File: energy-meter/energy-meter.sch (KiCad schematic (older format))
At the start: 9 parts, among them J1 Screw_Terminal_01x04, K1 G5RL-U1A-E, P1 PineNut, T1 AP-2500, T2 BV 202 0154, U9 GD32VF103

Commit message: continue changing schematic
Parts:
- removed R? (x3): 50R, 0.1%, Resistor_SMD:R_0603_1608Metric_Pad1.05x0.95mm_HandSolder, symbol Device:R
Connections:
- net CURRENT0: now reaches T1.1
- net CURRENT1: now reaches T1.2
- net VOLTAGE1: now reaches T2.6 (SA)
- net VOLTAGE0: now reaches T2.7 (SB)
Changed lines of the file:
@@
 F7 "TEMP1" I L 4500 5750 50
 F8 "VDDA" I R 5600 4950 50
-F9 "OUT0B" I R 5600 5350 50
-F10 "OUT1" I R 5600 5450 50
-F11 "IN1" I R 5600 5550 50
-F12 "IN0" I R 5600 5650 50
-F13 "DAC0" I L 4500 5550 50
-F14 "DAC1" I L 4500 5650 50
-F15 "OUT1_to_MCU" I L 4500 6150 50
-F16 "SCL" I L 4500 5150 50
-F17 "SDA" I L 4500 5250 50
-F18 "U10B_10k" I L 4500 6250 50
-F19 "OUT01_SHORT" I L 4500 6350 50
+F9 "DAC0" I L 4500 5550 50
+F10 "DAC1" I L 4500 5650 50
+F11 "OUT1_to_MCU" I L 4500 6150 50
+F12 "SCL" I L 4500 5150 50
+F13 "SDA" I L 4500 5250 50
+F14 "U10B_10k" I L 4500 6250 50
+F15 "OUT01_SHORT" I L 4500 6350 50
+F16 "CURRENT1" I R 5600 5600 50
+F17 "CURRENT0" I R 5600 5500 50
+F18 "VOLTAGE1" I R 5600 5400 50
+F19 "VOLTAGE0" I R 5600 5300 50
 $EndSheet
 $Comp
@@
 Text GLabel 7100 2950 0    50   Input ~ 0
 N
-$Comp
-L Device:R R?
-U 1 1 6094B5A5
-P 8300 3400
-AR Path="/602A3FC4/6094B5A5" Ref="R?"  Part="1"
-AR Path="/60514CC5/6094B5A5" Ref="R?"  Part="1"
-AR Path="/607B74C2/6094B5A5" Ref="R?"  Part="1"
-AR Path="/6094B5A5" Ref="R?"  Part="1"
-F 0 "R?" V 8093 3400 50  0000 C CNN
-F 1 "50R, 0.1%" V 8184 3400 50  0000 C CNN
-F 2 "Resistor_SMD:R_0603_1608Metric_Pad1.05x0.95mm_HandSolder" V 8230 3400 50  0001 C CNN
-F 3 "~" H 8300 3400 50  0001 C CNN
-	1    8300 3400
-	1    0    0    -1
-$EndComp
 Wire Wire Line
 	7600 3700 8300 3700
 Wire Wire Line
-	8300 3700 8300 3550
-Wire Wire Line
 	7600 3100 8300 3100
 Wire Wire Line
-	8300 3100 8300 3250
-$Comp
-L Device:R R?
-U 1 1 6094D567
-P 8150 2550
-AR Path="/602A3FC4/6094D567" Ref="R?"  Part="1"
-AR Path="/60514CC5/6094D567" Ref="R?"  Part="1"
-AR Path="/607B74C2/6094D567" Ref="R?"  Part="1"
-AR Path="/6094D567" Ref="R?"  Part="1"
-F 0 "R?" V 7943 2550 50  0000 C CNN
-F 1 "50R, 0.1%" V 8034 2550 50  0000 C CNN
-F 2 "Resistor_SMD:R_0603_1608Metric_Pad1.05x0.95mm_HandSolder" V 8080 2550 50  0001 C CNN
-F 3 "~" H 8150 2550 50  0001 C CNN
-	1    8150 2550
-	0    1    1    0
-$EndComp
-$Comp
-L Device:R R?
-U 1 1 6094DE74
-P 8400 2750
-AR Path="/602A3FC4/6094DE74" Ref="R?"  Part="1"
-AR Path="/60514CC5/6094DE74" Ref="R?"  Part="1"
-AR Path="/607B74C2/6094DE74" Ref="R?"  Part="1"
-AR Path="/6094DE74" Ref="R?"  Part="1"
-F 0 "R?" V 8193 2750 50  0000 C CNN
-F 1 "50R, 0.1%" V 8284 2750 50  0000 C CNN
-F 2 "Resistor_SMD:R_0603_1608Metric_Pad1.05x0.95mm_HandSolder" V 8330 2750 50  0001 C CNN
-F 3 "~" H 8400 2750 50  0001 C CNN
-	1    8400 2750
-	-1   0    0    1
-$EndComp
-Wire Wire Line
-	7900 2950 8400 2950
-Wire Wire Line
-	8400 2950 8400 2900
-Wire Wire Line
-	8400 2600 8400 2550
-Wire Wire Line
-	8400 2550 8300 2550
-Wire Wire Line
-	8000 2550 7900 2550
+	7900 2950 8300 2950
+Text Label 6050 5300 2    50   ~ 0
+VOLTAGE0
+Text Label 6050 5400 2    50   ~ 0
+VOLTAGE1
+Text Label 6050 5500 2    50   ~ 0
+CURRENT0
+Text Label 6050 5600 2    50   ~ 0
+CURRENT1
+Wire Wire Line
+	5600 5300 6050 5300
+Wire Wire Line
+	6050 5400 5600 5400
+Wire Wire Line
+	6050 5500 5600 5500
+Wire Wire Line
+	6050 5600 5600 5600
+Text Label 8300 2550 2    50   ~ 0
+VOLTAGE0
+Text Label 8300 2950 2    50   ~ 0
+VOLTAGE1
+Text Label 8300 3100 2    50   ~ 0
+CURRENT0
+Text Label 8300 3700 2    50   ~ 0
+CURRENT1
+Wire Wire Line
+	7900 2550 8300 2550
 $EndSCHEMATC

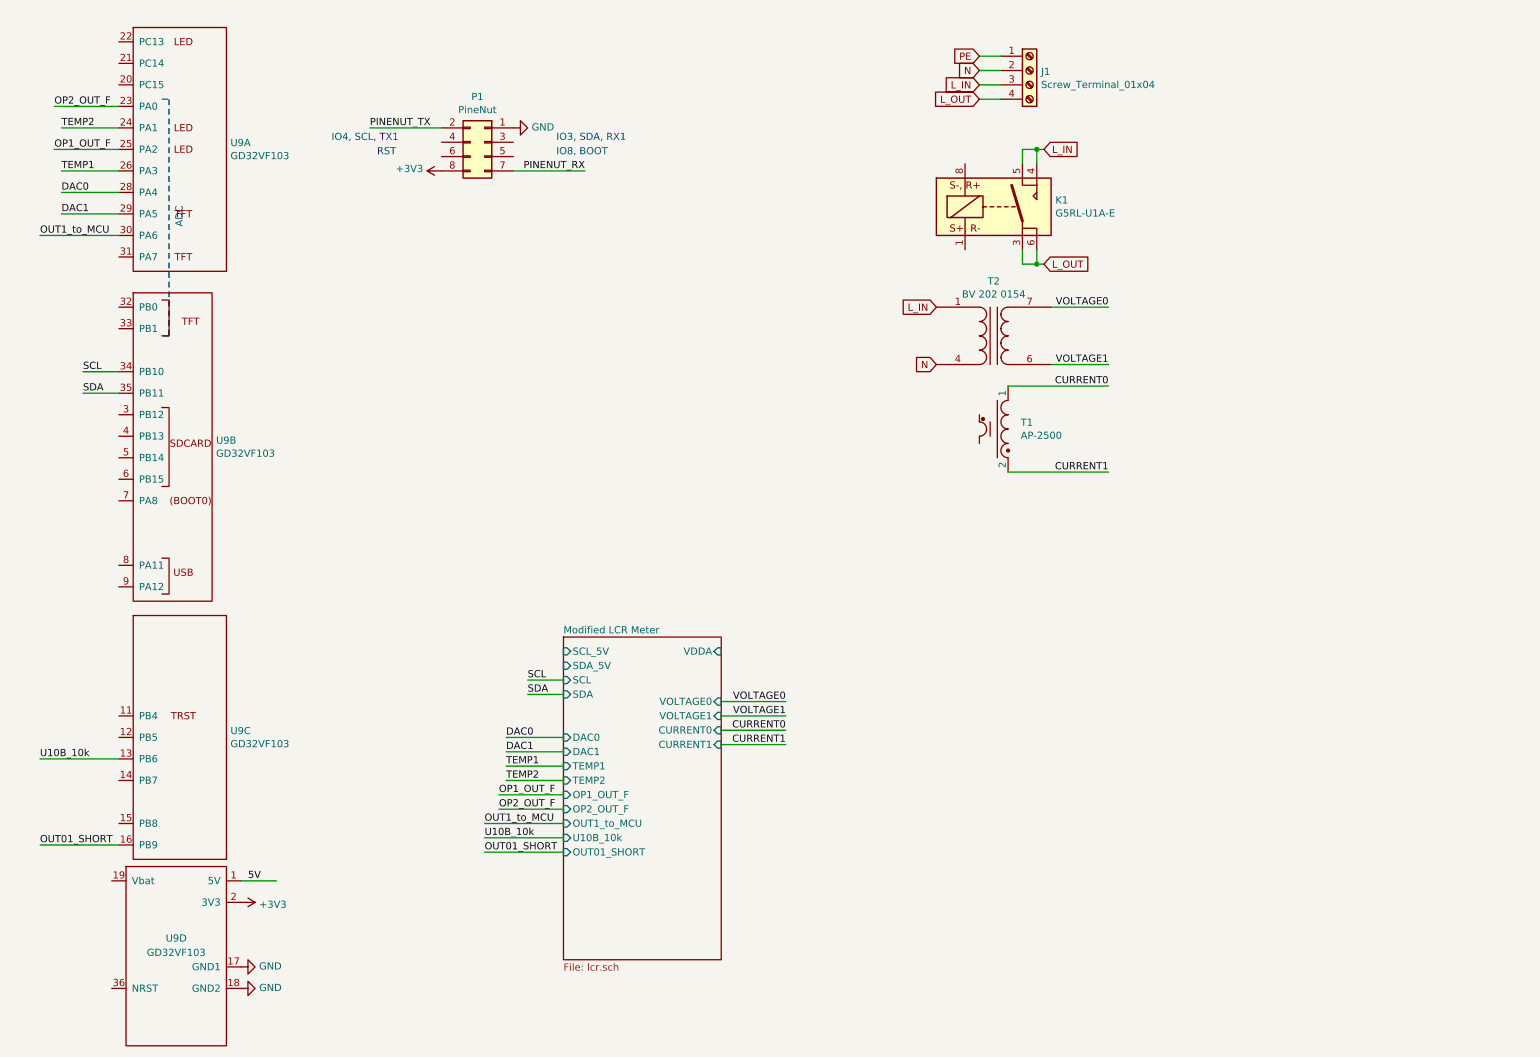
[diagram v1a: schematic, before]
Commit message: remove two of the opamps
We can measure the voltage without an amplifier so let's do it. The other
was used for the LCR outputs, which we don't have here.
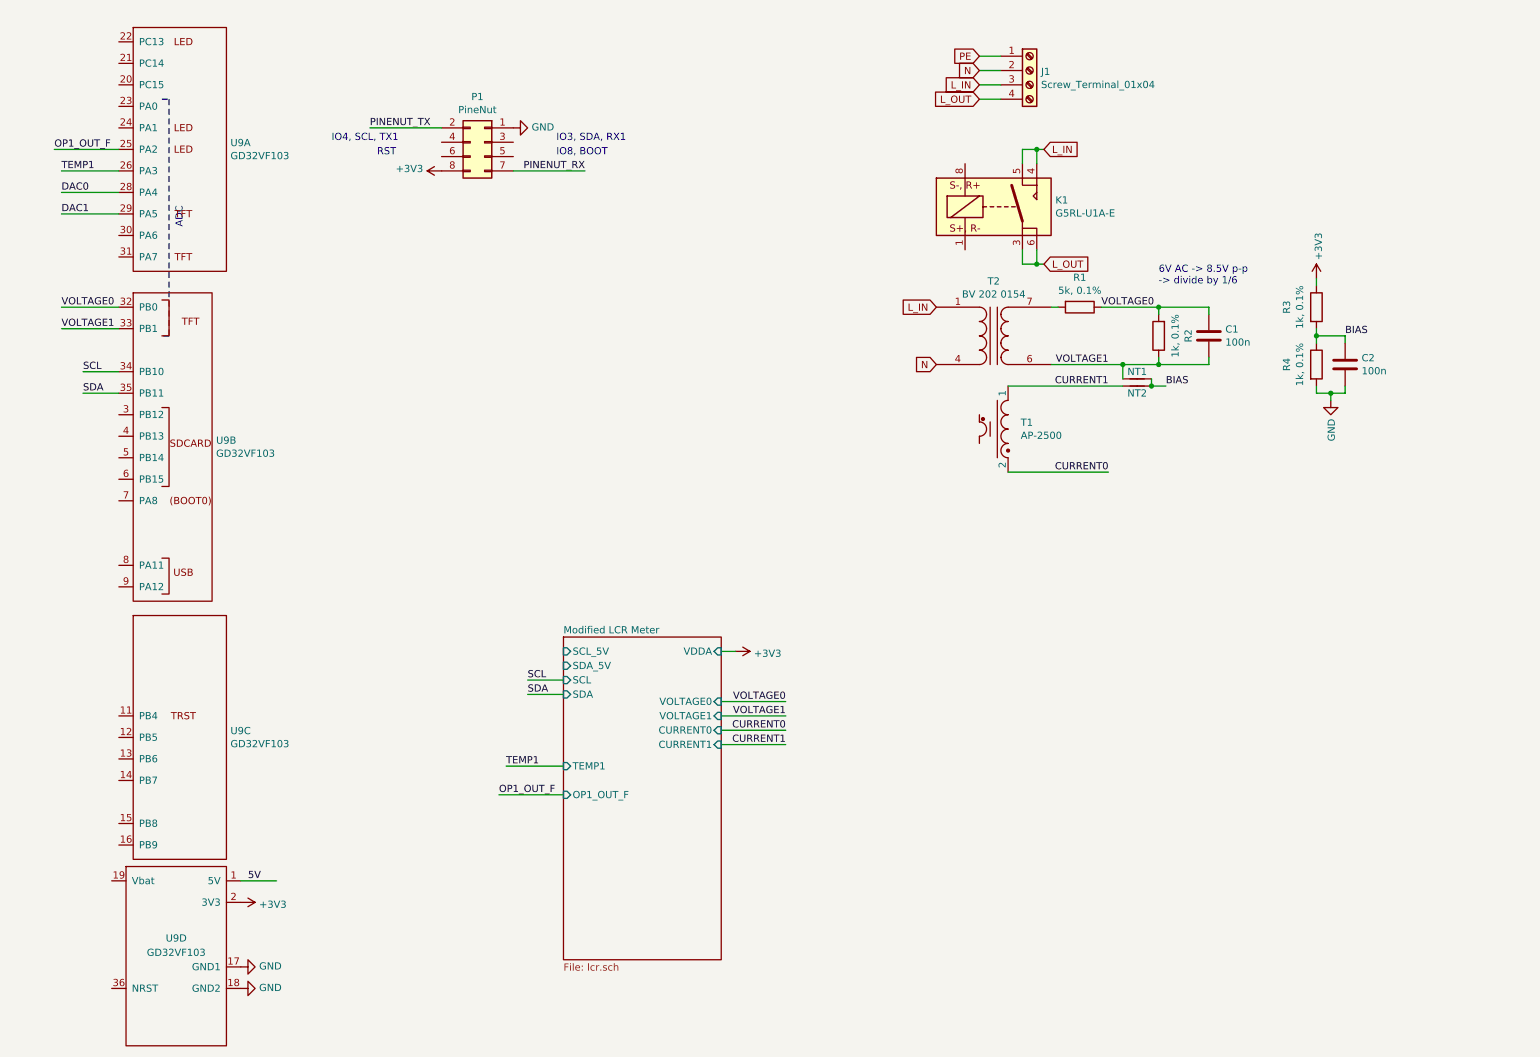
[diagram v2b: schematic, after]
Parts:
- added C1, C2: 100n, Capacitor_SMD:C_0603_1608Metric_Pad1.05x0.95mm_HandSolder, symbol Device:C
- added NT1, NT2: Net-Tie_2, NetTie:NetTie-2_SMD_Pad0.5mm, symbol Device:Net-Tie_2
- added R1: 5k, 0.1%, Resistor_SMD:R_0603_1608Metric_Pad1.05x0.95mm_HandSolder, symbol Device:R
- added R2, R3, R4: 1k, 0.1%, Resistor_SMD:R_0603_1608Metric_Pad1.05x0.95mm_HandSolder, symbol Device:R
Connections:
- net +3V3: now also R3.1
- net CURRENT0: now also T1.2; no longer T1.1
- net CURRENT1: now also T1.1, NT2.1; no longer T1.2
- net GND: now also C2.2, R4.2
- net VOLTAGE0: now also U9.32 (PB0), C1.1, R1.1, R2.2; no longer T2.7 (SB)
- net VOLTAGE1: now also U9.33 (PB1), C1.2, NT1.2, R2.1
- net OP2_OUT_F: no longer names the net of U9.23 (PA0)
- net OUT01_SHORT: no longer names the net of U9.16 (PB9)
- net OUT1_to_MCU: no longer names the net of U9.30 (PA6)
- net TEMP2: no longer names the net of U9.24 (PA1)
- net U10B_10k: no longer names the net of U9.13 (PB6)
- new net: R1.2, T2.7 (SB)
- new net BIAS: C2.1, NT1.1, NT2.2, R3.2, R4.1
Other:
- note added: "6V AC -> 8.5V p-p\n-> divide by 1/6"

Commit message: everything done except current measurement
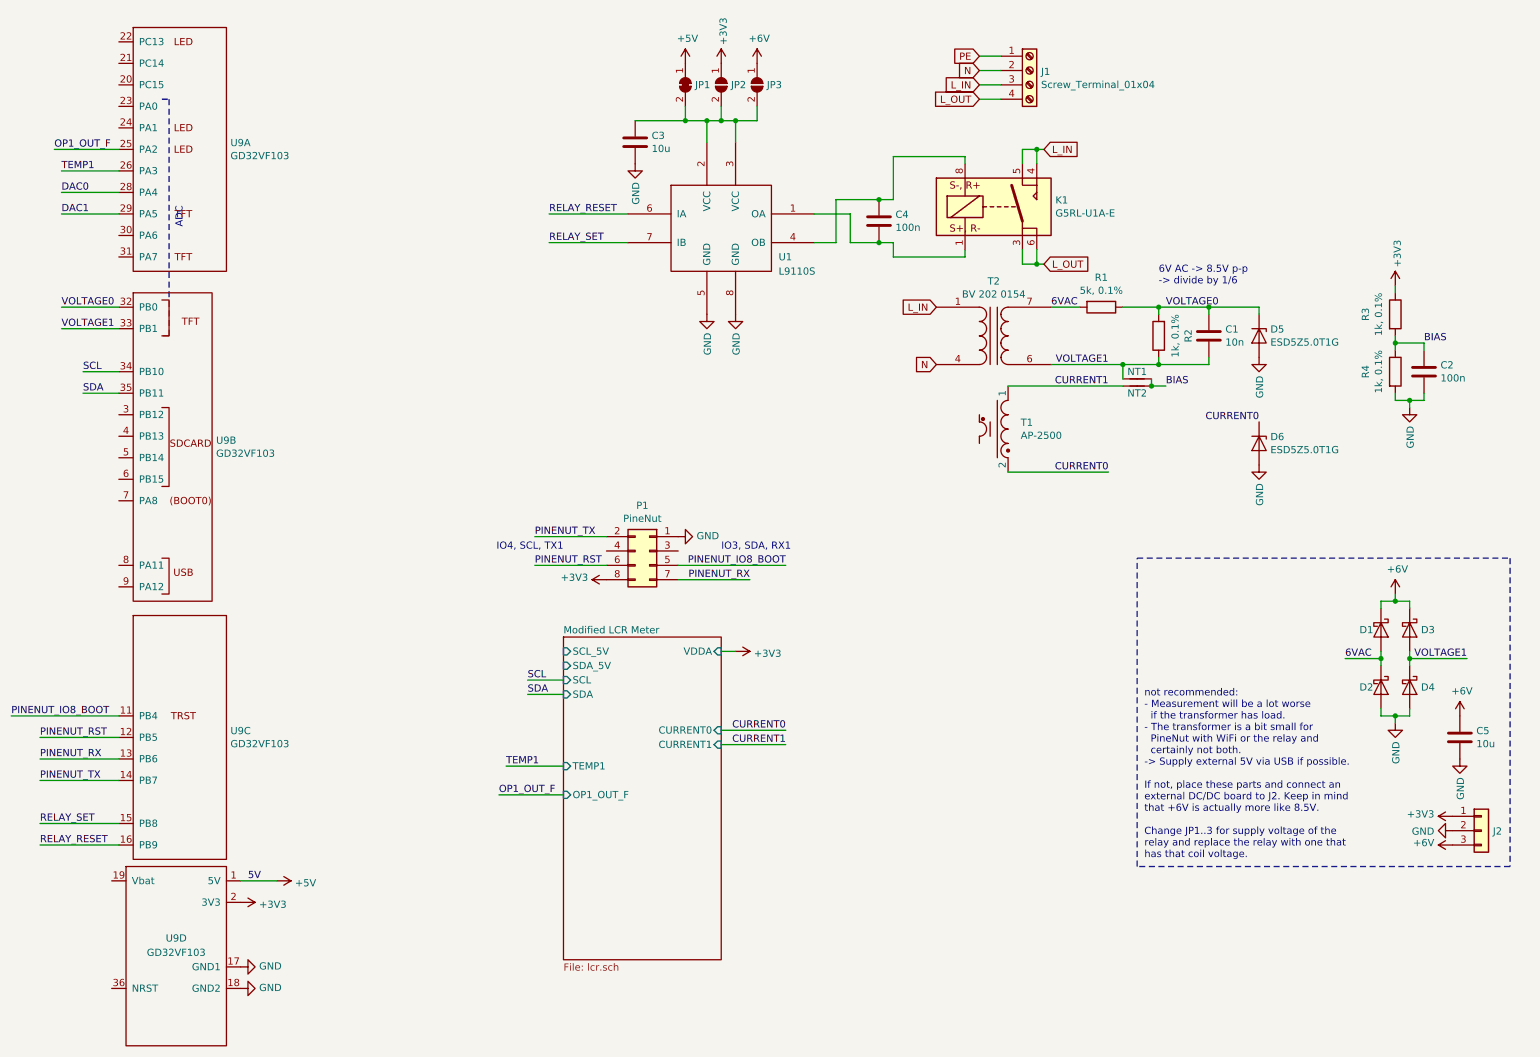
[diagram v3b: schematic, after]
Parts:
- added C3, C5: 10u, Capacitor_SMD:C_0805_2012Metric_Pad1.15x1.40mm_HandSolder, symbol Device:C
- added C4: 100n, Capacitor_SMD:C_0603_1608Metric_Pad1.05x0.95mm_HandSolder, symbol Device:C
- added D1, D2, D3, D4: D_Schottky, Diode_SMD:D_SMA_Handsoldering, symbol Device:D_Schottky
- added D5, D6: ESD5Z5.0T1G, Diode_SMD:D_SOD-523, symbol Device:D_Zener
- added J2: Conn_01x03, Connector_PinHeader_2.54mm:PinHeader_1x03_P2.54mm_Horizontal, symbol Connector_Generic:Conn_01x03
- added JP1: SolderJumper_2_Bridged, Jumper:SolderJumper-2_P1.3mm_Bridged_RoundedPad1.0x1.5mm, symbol Jumper:SolderJumper_2_Bridged
- added JP2, JP3: SolderJumper_2_Open, Jumper:SolderJumper-2_P1.3mm_Open_RoundedPad1.0x1.5mm, symbol Jumper:SolderJumper_2_Open
- added U1: L9110S, Package_SO:SOP-8_3.76x4.96mm_P1.27mm, symbol energy-meter:L9110S
- C1: value 100n -> 10n
- J1: TME (none) -> https://www.tme.eu/de/details/dg35c-b-04p/klemmleisten-fur-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
- K1: TME (none) -> https://www.tme.eu/de/details/g5rl-u1a-e-5dc/elektromagneti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
- T1: TME (none) -> https://www.tme.eu/de/details/ap-2500/stromwandler/talema/
- T2: TME (none) -> https://www.tme.eu/de/details/bv2020154/pcb-transformatoren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
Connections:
- net +3V3: now also J2.1 (Pin_1), JP2.1 (A)
- net CURRENT0: now also D6.1 (K)
- net GND: now also C3.2, C5.2, D2.2 (A), D4.2 (A), D5.2 (A), D6.2 (A), J2.2 (Pin_2), U1.5 (GND), U1.8 (GND)
- net PINENUT_RX: now also U9.13 (PB6)
- net PINENUT_TX: now also U9.14 (PB7)
- net VOLTAGE0: now also D5.1 (K)
- net VOLTAGE1: now also D3.2 (A), D4.1 (K)
- net PINENUT_IO8_BOOT: now reaches U9.11 (PB4)
- net PINENUT_IO8_BOOT: now also P1.5 (Pin_5)
- net PINENUT_RST: now reaches U9.12 (PB5)
- net PINENUT_RST: now also P1.6 (Pin_6)
- net RELAY_SET: now reaches U9.15 (PB8)
- net RELAY_SET: now also U1.7 (IB)
- net RELAY_RESET: now reaches U9.16 (PB9)
- net RELAY_RESET: now also U1.6 (IA)
- net at K1.1: now also C4.2, U1.1 (OA)
- net at K1.8: now also C4.1, U1.4 (OB)
- net 6VAC: now reaches R1.2, T2.7 (SB)
- net 6VAC: now also D1.2 (A), D2.1 (K)
- net 5V renamed +5V
- net +5V: now also JP1.1 (A)
- new net: C3.1, JP1.2 (B), JP2.2 (B), JP3.2 (B), U1.2 (VCC), U1.3 (VCC)
- new net +6V: C5.1, D1.1 (K), D3.1 (K), J2.3 (Pin_3), JP3.1 (A)
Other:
- note added: "not recommended:\n- Measurement will be a lot worse\n if the transformer has load.\n- The transformer is a bit small for\n PineNut with WiFi or the relay and\n certainly not both.\n-> Supply external 5V via USB if possible.\n\nIf not, place these parts and connect an\nexternal DC/DC board to J2. Keep in mind\nthat +6V is actually more like 8.5V.\n\nChange JP1..3 for supply voltage of the\nrelay a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"
- note removed: "IO8, BOOT"
- note removed: "RST"
- moved on the sheet: C2, P1, R1, R3, R4
